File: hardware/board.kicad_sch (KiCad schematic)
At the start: 7 parts, among them U1 STM32F446RETx

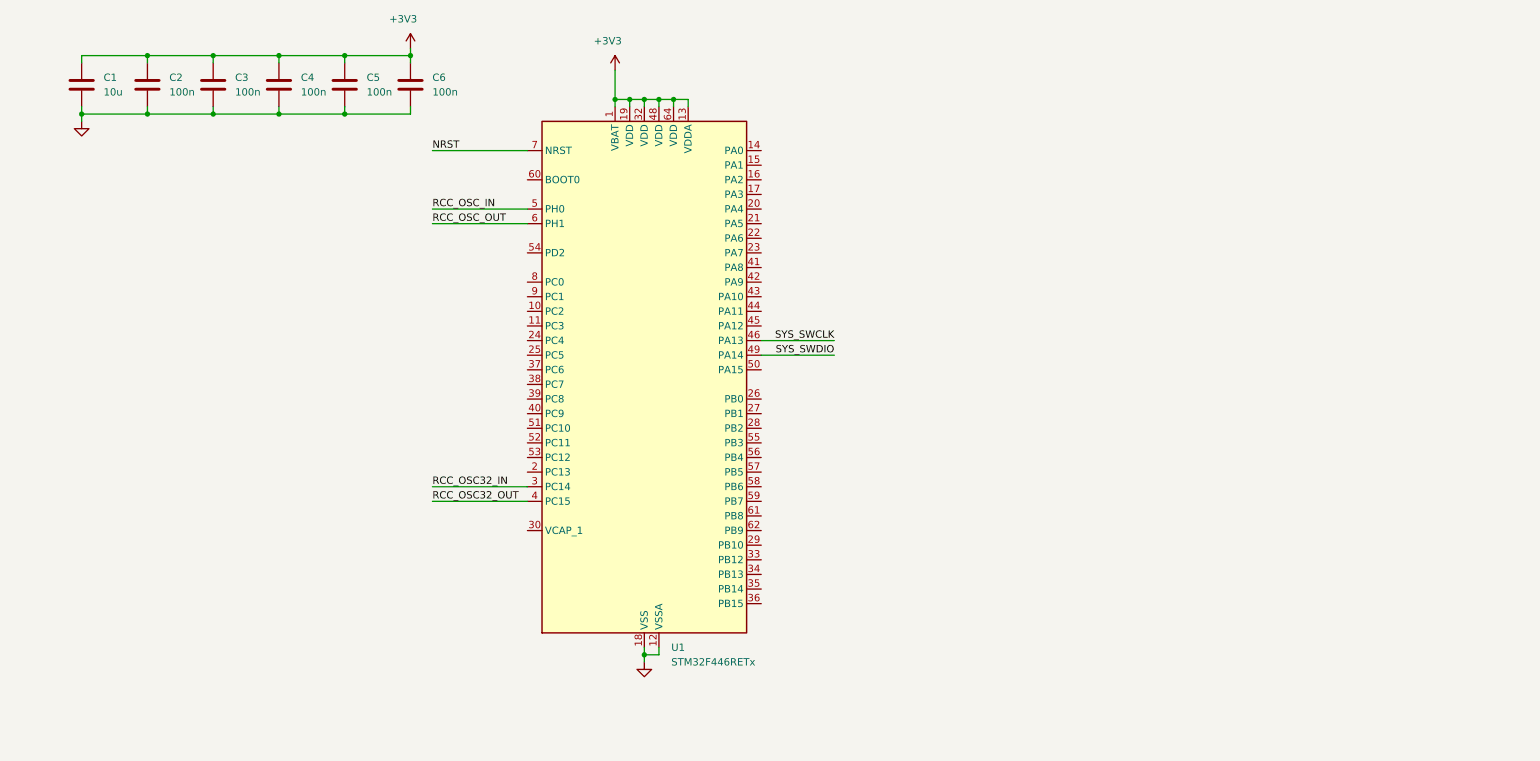
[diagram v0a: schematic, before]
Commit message: added LSE and PWR to schematic
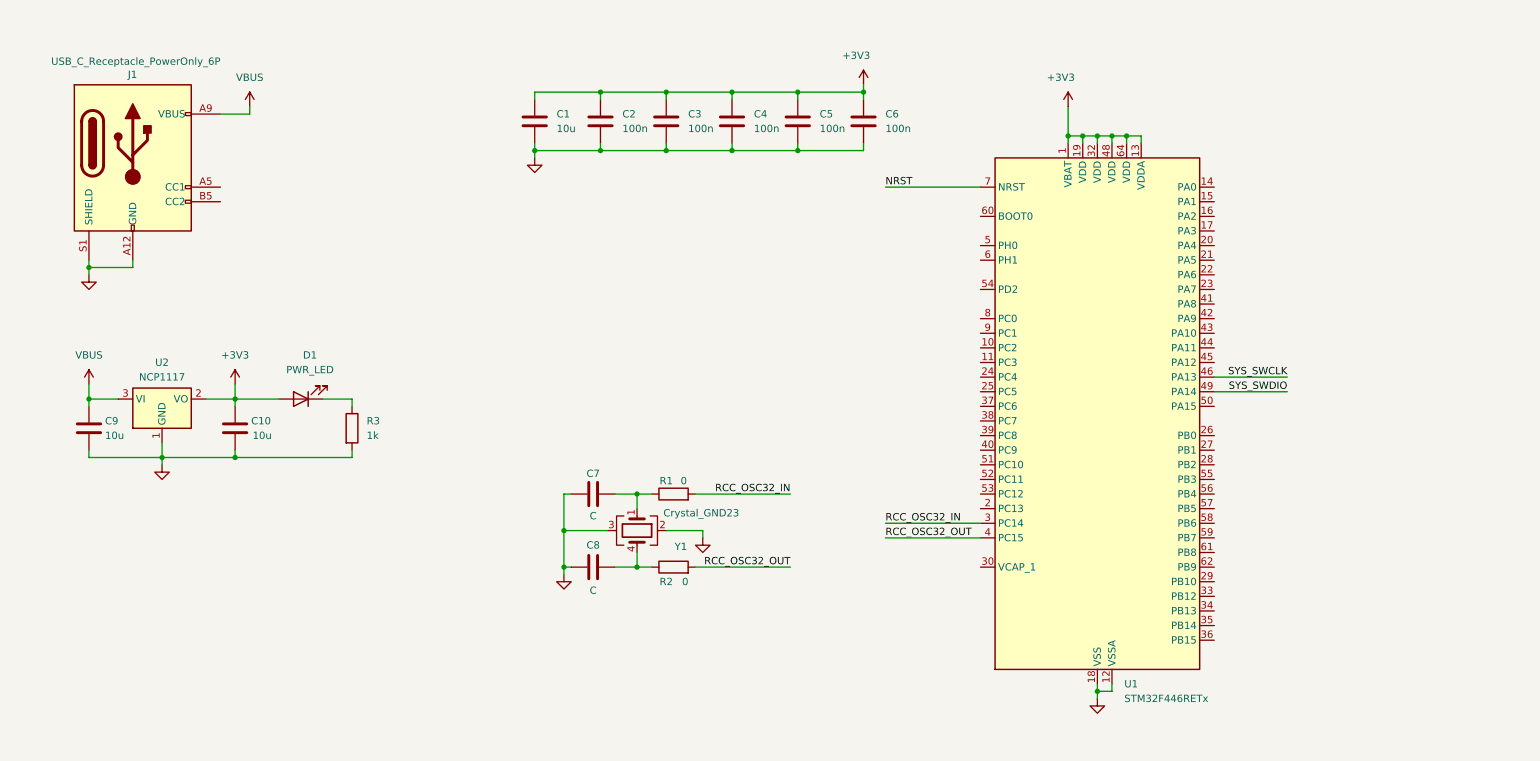
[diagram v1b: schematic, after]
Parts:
- added C10, C9: 10u, Capacitor_SMD:C_0805_2012Metric_Pad1.18x1.45mm_HandSolder, symbol Device:C
- added C7, C8: C, Capacitor_SMD:C_0805_2012Metric_Pad1.18x1.45mm_HandSolder, symbol Device:C
- added D1: PWR_LED, LED_SMD:LED_0805_2012Metric_Pad1.15x1.40mm_HandSolder, symbol Device:LED
- added J1: USB_C_Receptacle_PowerOnly_6P, Connector_USB:USB_C_Receptacle_GCT_USB4125-xx-x-0190_6P_TopMnt_Horizontal, symbol Connector:USB_C_Receptacle_PowerOnly_6P
- added R1, R2: 0, Resistor_SMD:R_0805_2012Metric_Pad1.20x1.40mm_HandSolder, symbol Device:R
- added R3: 1k, Resistor_SMD:R_0805_2012Metric_Pad1.20x1.40mm_HandSolder, symbol Device:R
- added U2: NCP1117, Package_TO_SOT_SMD:SOT-223-3_TabPin2, symbol Regulator_Linear:NCP1117-3.3_SOT223
- added Y1: Crystal_GND23, Crystal:Crystal_SMD_Abracon_ABS25-4Pin_8.0x3.8mm, symbol Device:Crystal_GND23
- C1: footprint Capacitor_SMD:C_0201_0603Metric_Pad0.64x0.40mm_HandSolder -> Capacitor_SMD:C_0805_2012Metric_Pad1.18x1.45mm_HandSolder
- C2, C3, C4, C5, C6: footprint (none) -> Capacitor_SMD:C_0805_2012Metric_Pad1.18x1.45mm_HandSolder
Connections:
- net +3V3: now also C10.1, D1.2 (A), U2.2 (VO)
- net GND: now also C10.2, C7.1, C8.1, C9.2, J1.A12 (GND), J1.B12 (GND), J1.S1 (SHIELD), R3.2, U2.1 (GND), Y1.2, Y1.3
- net RCC_OSC32_IN: now also R1.2
- net RCC_OSC32_OUT: now also R2.2
- net RCC_OSC_IN: no longer names the net of U1.5 (PH0)
- net RCC_OSC_OUT: no longer names the net of U1.6 (PH1)
- new net: D1.1 (K), R3.1
- new net: C8.2, R2.1, Y1.4
- new net: C7.2, R1.1, Y1.1
- new net VBUS: C9.1, J1.A9 (VBUS), J1.B9 (VBUS), U2.3 (VI)
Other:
- moved on the sheet: C1, C2, C3, C4, C5, C6, U1

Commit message: added mcu circuitry and updated power circuitry
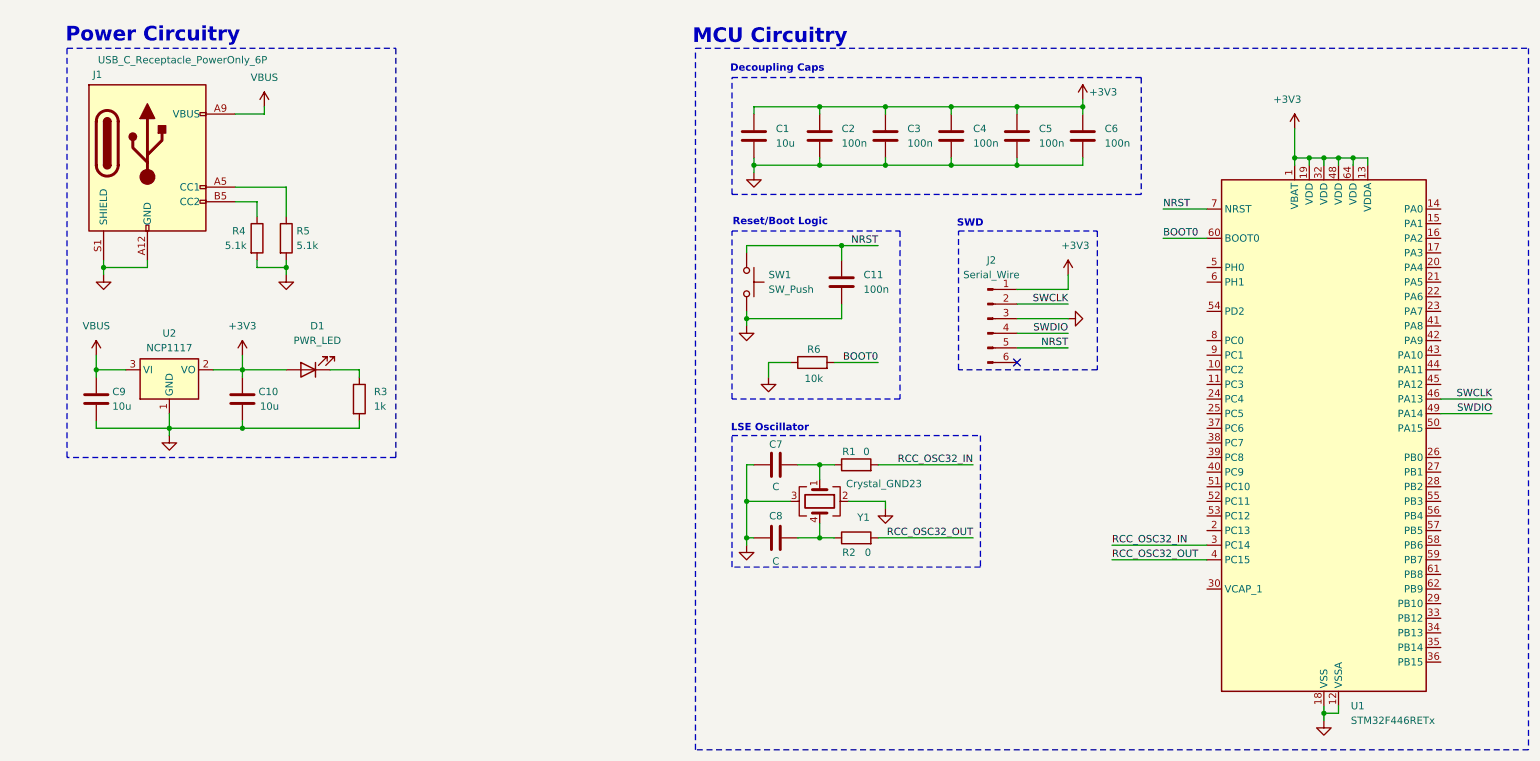
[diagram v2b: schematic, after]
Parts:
- added C11: 100n, Capacitor_SMD:C_0805_2012Metric_Pad1.18x1.45mm_HandSolder, symbol Device:C
- added J2: Serial_Wire, Connector_PinHeader_2.54mm:PinHeader_1x06_P2.54mm_Vertical, symbol Connector:Conn_01x06_Pin
- added R4, R5: 5.1k, symbol Device:R
- added R6: 10k, Resistor_SMD:R_0805_2012Metric_Pad1.20x1.40mm_HandSolder, symbol Device:R
- added SW1: SW_Push, symbol Switch:SW_Push
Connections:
- net +3V3: now also J2.1 (Pin_1)
- net GND: now also C11.2, J2.3 (Pin_3), R4.2, R5.2, R6.1, SW1.2
- net NRST: now also C11.1, J2.5 (Pin_5), SW1.1
- net BOOT0: now reaches U1.60 (BOOT0)
- net BOOT0: now also R6.2
- net at J1.A5 (CC1): now also R5.1
- net at J1.B5 (CC2): now also R4.1
- net SYS_SWCLK renamed SWCLK
- net SWCLK: now also J2.2 (Pin_2)
- net SYS_SWDIO renamed SWDIO
- net SWDIO: now also J2.4 (Pin_4)
- no-connect marks 0 -> 1
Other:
- note added: "Decoupling Caps"
- note added: "LSE Oscillator"
- note added: "MCU Circuitry"
- note added: "Power Circuitry"
- note added: "Reset/Boot Logic"
- note added: "SWD"
- moved on the sheet: C1, C10, C2, C3, C4, C5, C6, C7, C8, C9, D1, J1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
